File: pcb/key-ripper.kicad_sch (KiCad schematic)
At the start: 205 parts, among them J1 Conn_01x03, SW1 ESC, SW10 F9, SW11 F10, SW12 F11, SW13 F12, SW14 TILDE, SW15 1, SW16 2, SW17 3, SW18 4, SW19 5, SW2 F1, SW20 6, SW21 7, SW22 8, SW23 9, SW24 0, SW25 -, SW26 =, SW27 BACKSPACE, SW28 TAB, SW29 Q, SW3 F2, SW30 W, SW31 E, SW32 R, SW33 T, SW34 Y, SW35 U, SW36 I, SW37 O, SW38 P, SW39 [, SW4 F3, SW40 ], SW41 \, SW42 CAPS, SW43 A, SW44 S, SW45 D, SW46 F, SW47 G, SW48 H, SW49 J, SW5 F4, SW50 K, SW51 L, SW52 ;, SW53 ', SW54 ENTER, SW55 L_SHIFT, SW56 Z, SW57 X, SW58 C, SW59 V, SW6 F5, SW60 B, SW61 N, SW62 M, SW63 ,, SW64 ., SW65 /, SW66 UP, SW67 FN, SW68 BL_CTRL, SW69 L_ALT, SW7 F6, SW70 L_CMD, SW71 SPACE, SW72 R_CMD, SW73 LEFT, SW74 DOWN, SW75 RIGHT, SW8 F7, SW9 F8, U1 RP2040, U2 TYPE-C-31-M-12, U3 XC6206PxxxMR, U4 W25Q128JVS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

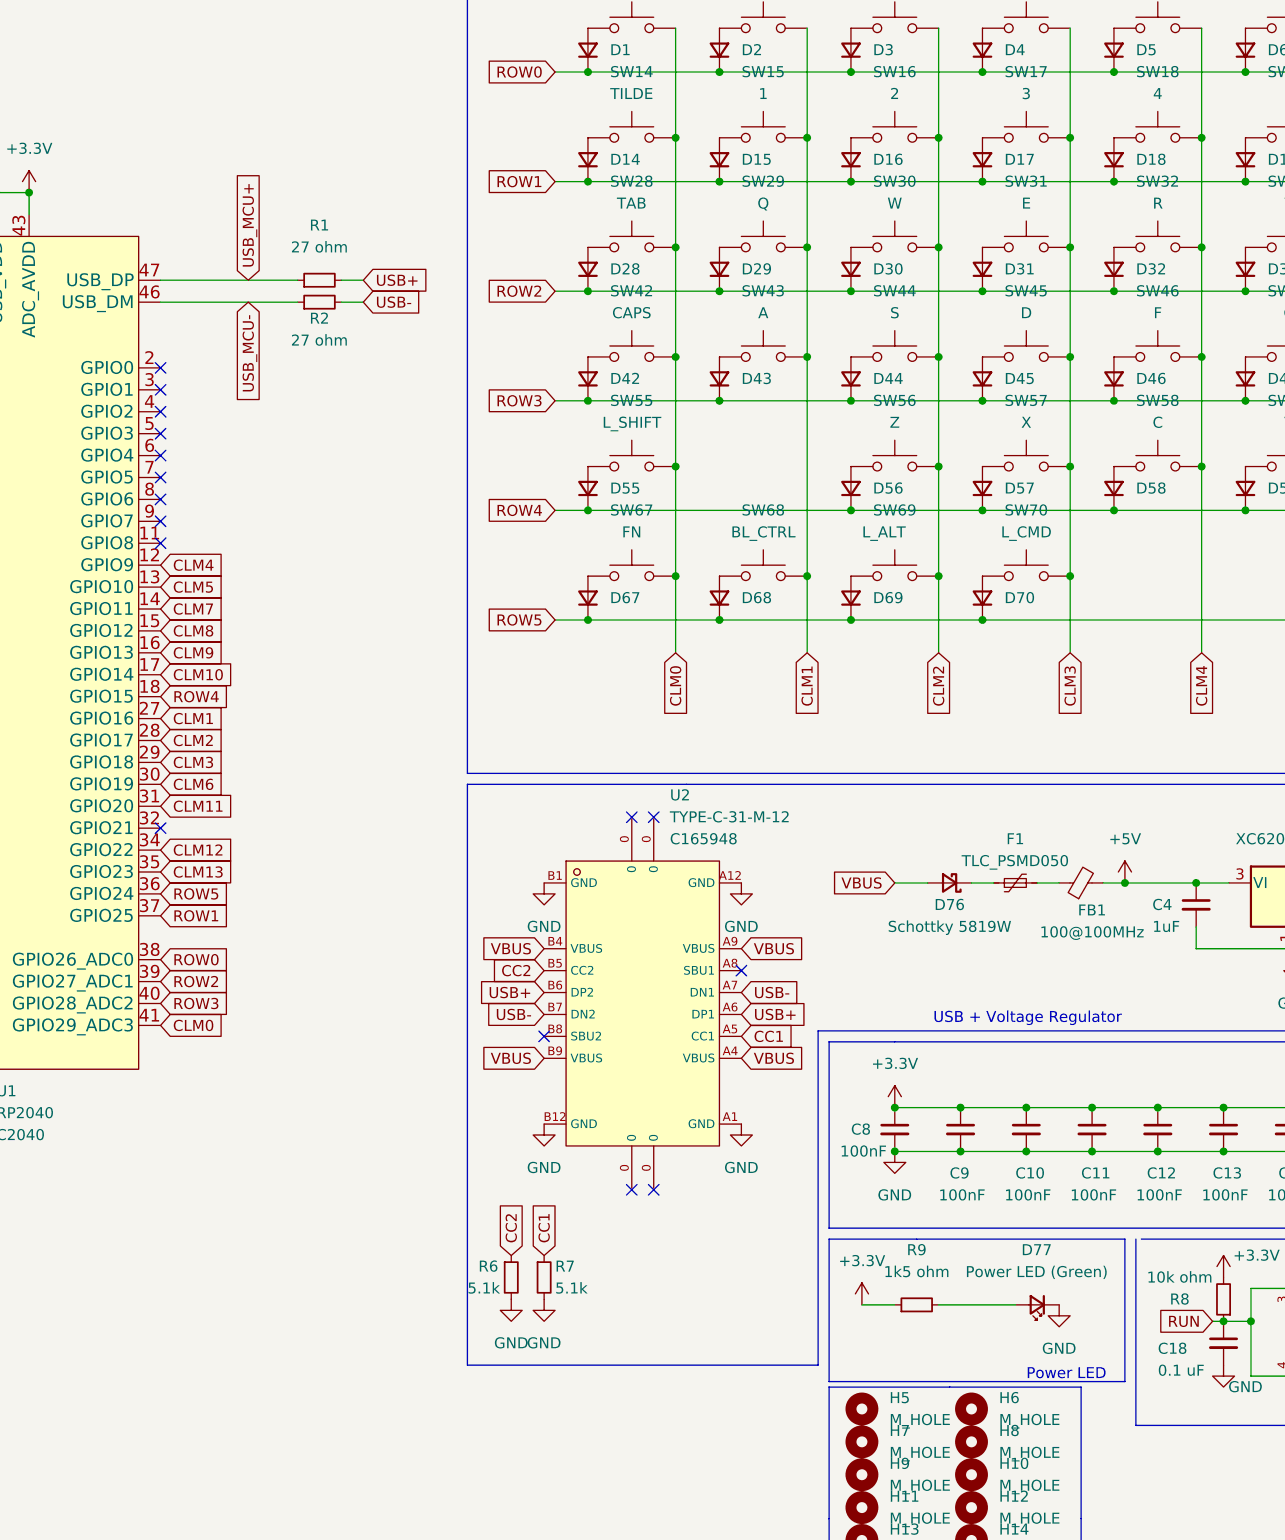
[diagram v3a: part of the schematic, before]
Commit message: Turn GPIO 2 into a user LED
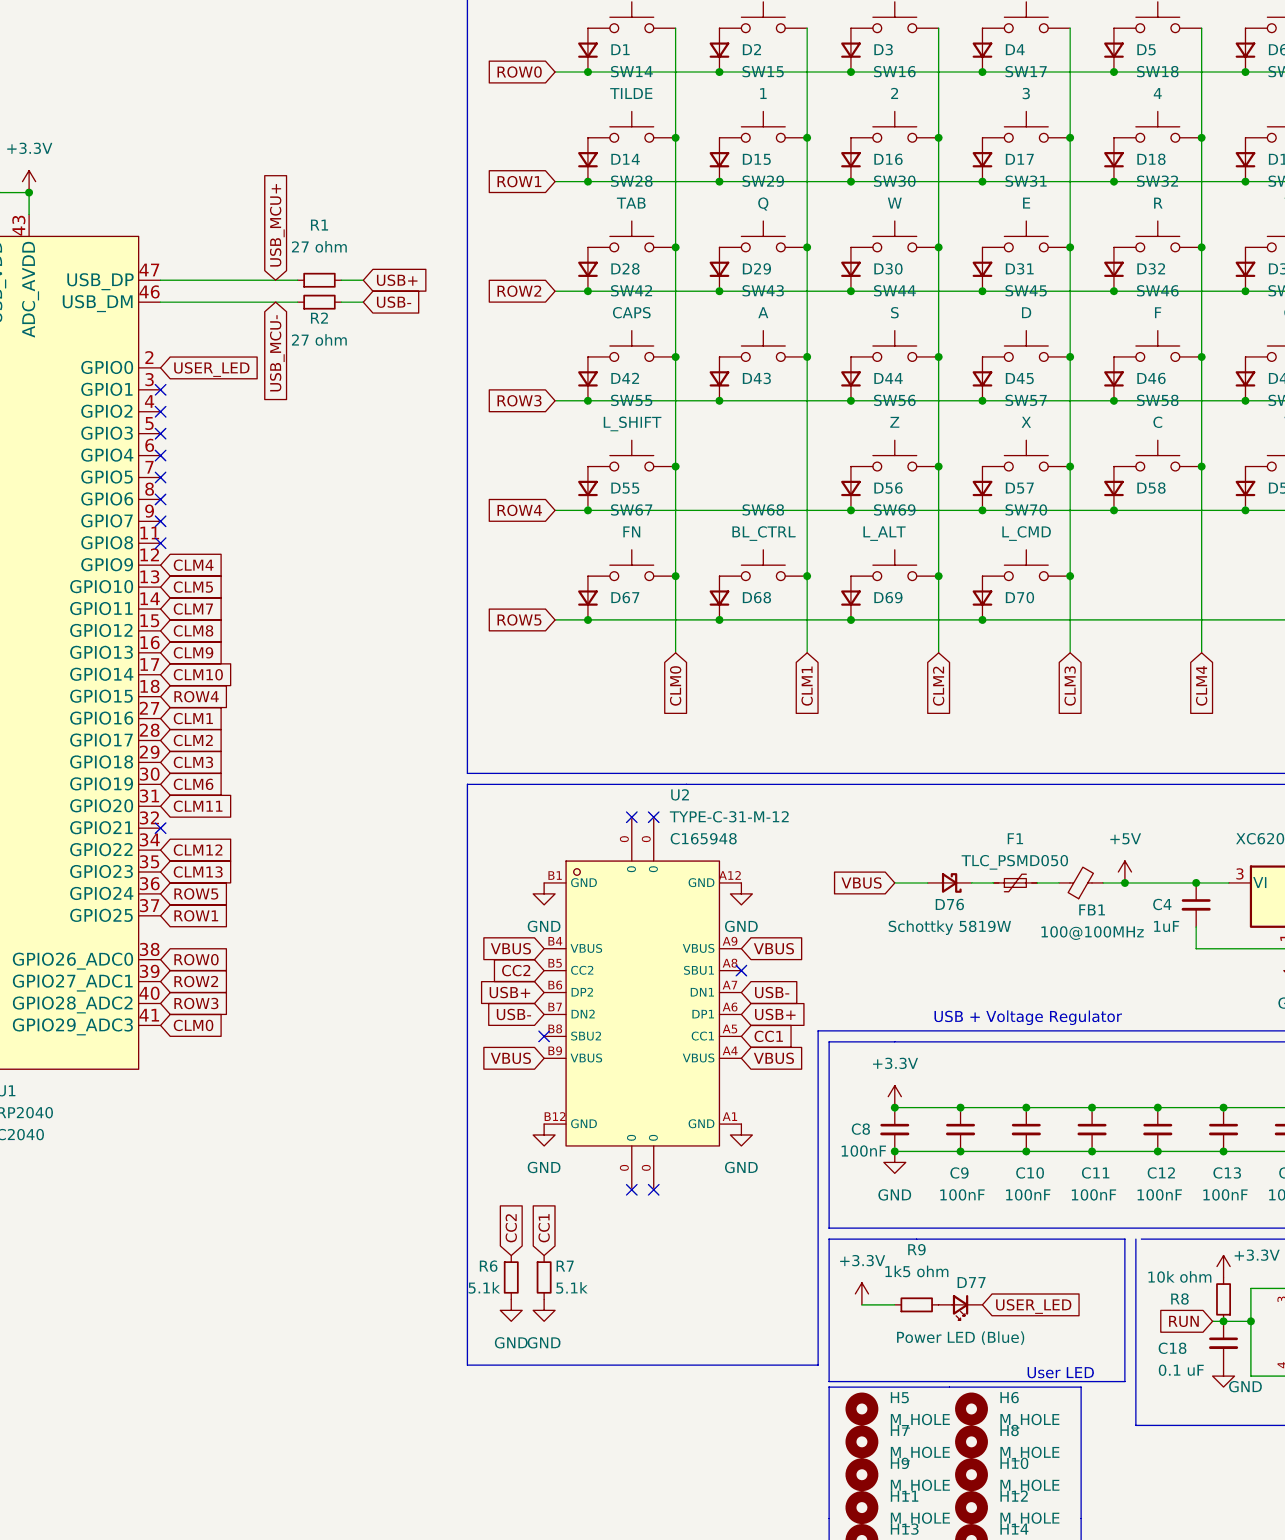
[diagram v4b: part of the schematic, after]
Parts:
- D77: value Power LED (Green) -> Power LED (Blue)
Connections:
- net GND: no longer D77.1 (K)
- net USER_LED: now reaches U1.2 (GPIO0)
- net USER_LED: now also D77.1 (K)
- no-connect marks 16 -> 15
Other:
- note added: "User LED"
- note removed: "Power LED"
- moved on the sheet: D77
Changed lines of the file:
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@@
   (no_connect (at -22.86 73.66))
   (no_connect (at -22.86 71.12))
-  (no_connect (at -22.86 63.5))
   (no_connect (at -22.86 116.84))
   (no_connect (at -22.86 68.58))
@@
     (stroke (width 0) (type default) (color 0 0 0 0))
   )
-  (wire (pts (xy 67.31 172.085) (xy 76.2 172.085))
-    (stroke (width 0) (type default) (color 0 0 0 0))
-  )
   (wire (pts (xy 118.11 54.61) (xy 133.35 54.61))
     (stroke (width 0) (type default) (color 0 0 0 0))
@@
     (effects (font (size 1.27 1.27)) (justify left bottom))
   )
-  (text "Power LED" (at 77.47 180.975 0)
+  (text "User LED" (at 77.47 180.975 0)
     (effects (font (size 1.27 1.27)) (justify left bottom))
   )
@@
     )
   )
-  (global_label "USB_MCU+" (shape input) (at -12.7 53.34 90) (fields_autoplaced)
+  (global_label "USB_MCU+" (shape input) (at -9.525 53.34 90) (fields_autoplaced)
     (effects (font (size 1.27 1.27)) (justify left))
-    (property "Intersheet References" "${INTERSHEET_REFS}" (id 0) (at -12.7794 40.525 90)
+    (property "Intersheet References" "${INTERSHEET_REFS}" (id 0) (at -9.6044 40.525 90)
       (effects (font (size 1.27 1.27)) (justify left) hide)
     )
@@
     )
   )
+  (global_label "USER_LED" (shape input) (at -22.86 63.5 0) (fields_autoplaced)
+    (effects (font (size 1.27 1.27)) (justify left))
+    (property "Intersheet References" "${INTERSHEET_REFS}" (id 0) (at -11.0731 63.4206 0)
+      (effects (font (size 1.27 1.27)) (justify left) hide)
+    )
+  )
   (global_label "CLM4" (shape input) (at 97.79 96.52 270) (fields_autoplaced)
     (effects (font (size 1.27 1.27)) (justify right))
@@
     )
   )
-  (global_label "USB_MCU-" (shape input) (at -12.7 55.88 270) (fields_autoplaced)
+  (global_label "USB_MCU-" (shape input) (at -9.525 55.88 270) (fields_autoplaced)
     (effects (font (size 1.27 1.27)) (justify right))
-    (property "Intersheet References" "${INTERSHEET_REFS}" (id 0) (at -12.7794 68.695 90)
+    (property "Intersheet References" "${INTERSHEET_REFS}" (id 0) (at -9.6044 68.695 90)
       (effects (font (size 1.27 1.27)) (justify right) hide)
     )
@@
     )
   )
+  (global_label "USER_LED" (shape input) (at 72.39 172.085 0) (fields_autoplaced)
+    (effects (font (size 1.27 1.27)) (justify left))
+    (property "Intersheet References" "${INTERSHEET_REFS}" (id 0) (at 84.1769 172.0056 0)
+      (effects (font (size 1.27 1.27)) (justify left) hide)
+    )
+  )
   (global_label "RUN" (shape input) (at -86.36 116.84 180) (fields_autoplaced)
     (effects (font (size 1.27 1.27)) (justify right))
@@
     (pin "2")
   )
-  (symbol (lib_id "power:GND") (at 81.28 172.085 0) (unit 1)
-    (in_bom yes) (on_board yes) (fields_autoplaced)
-    (property "Reference" "#PWR031" (id 0) (at 81.28 178.435 0)
-      (effects (font (size 1.27 1.27)) hide)
-    )
-    (property "Value" "GND" (id 1) (at 81.28 177.165 0))
-    (property "Footprint" "" (id 2) (at 81.28 172.085 0)
-      (effects (font (size 1.27 1.27)) hide)
-    )
-    (property "Datasheet" "" (id 3) (at 81.28 172.085 0)
-      (effects (font (size 1.27 1.27)) hide)
-    )
-    (pin "1")
-  )
   (symbol (lib_id "Device:D_Small") (at 87.63 52.07 90) (unit 1)
     (in_bom yes) (on_board yes)
@@
     (pin "2")
   )
-  (symbol (lib_id "Device:LED_Small") (at 78.74 172.085 180) (unit 1)
-    (in_bom yes) (on_board yes) (fields_autoplaced)
-    (property "Reference" "D77" (id 0) (at 78.6765 165.735 0))
-    (property "Value" "Power LED (Green)" (id 1) (at 78.6765 168.275 0))
-    (property "Footprint" "LED_SMD:LED_0805_2012Metric" (id 2) (at 78.74 172.085 90)
+  (symbol (lib_id "Device:LED_Small") (at 69.85 172.085 180) (unit 1)
+    (in_bom yes) (on_board yes)
+    (property "Reference" "D77" (id 0) (at 71.12 169.545 0))
+    (property "Value" "Power LED (Blue)" (id 1) (at 69.85 175.895 0))
+    (property "Footprint" "LED_SMD:LED_0805_2012Metric" (id 2) (at 69.85 172.085 90)
       (effects (font (size 1.27 1.27)) hide)
     )
-    (property "Datasheet" "~" (id 3) (at 78.74 172.085 90)
+    (property "Datasheet" "~" (id 3) (at 69.85 172.085 90)
       (effects (font (size 1.27 1.27)) hide)
     )
@@
       (reference "#PWR030") (unit 1) (value "+3.3V") (footprint "")
     )
-    (path "/2cb114ba-1938-4b9e-8b57-e5a613f9de7f"
-      (reference "#PWR031") (unit 1) (value "GND") (footprint "")
-    )
     (path "/cdc9f184-a98f-4194-a3dd-613cbf52294c"
       (reference "#PWR032") (unit 1) (value "GND") (footprint "")
@@
     )
     (path "/f01c71a7-46e2-4e2a-a493-f3aa185e40b3"
-      (reference "D77") (unit 1) (value "Power LED (Green)") (footprint "LED_SMD:LED_0805_2012Metric")
+      (reference "D77") (unit 1) (value "Power LED (Blue)") (footprint "LED_SMD:LED_0805_2012Metric")
     )
     (path "/b1435a2c-b9ff-468c-9db6-b6d7bca7609e"

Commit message: Use the soldered MX footprint instead of kailh hotswap footprint
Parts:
- SW1, SW10, SW11, SW12, SW13, SW14, SW15, SW16, SW17, SW18, SW19, SW2, SW20, SW21, SW22, SW23, SW24, SW25, SW26, SW29, SW3, SW30, SW31, SW32, SW33, SW34, SW35, SW36, SW37, SW38, SW39, SW4, SW40, SW43, SW44, SW45, SW46, SW47, SW48, SW49, SW5, SW50, SW51, SW52, SW53, SW56, SW57, SW58, SW59, SW6, SW60, SW61, SW62, SW63, SW64, SW65, SW66, SW67, SW68, SW69, SW7, SW73, SW74, SW75, SW8, SW9: footprint Switch_Keyboard_Hotswap_Kailh:SW_Hotswap_Kailh_MX_1.00u -> Switch_Keyboard_Cherry_MX:SW_Cherry_MX_PCB_1.00u
- SW27: footprint Switch_Keyboard_Hotswap_Kailh:SW_Hotswap_Kailh_MX_2.00u -> Switch_Keyboard_Cherry_MX:SW_Cherry_MX_PCB_2.00u
- SW28, SW41: footprint Switch_Keyboard_Hotswap_Kailh:SW_Hotswap_Kailh_MX_1.50u -> Switch_Keyboard_Cherry_MX:SW_Cherry_MX_PCB_1.50u
- SW42: footprint Switch_Keyboard_Hotswap_Kailh:SW_Hotswap_Kailh_MX_1.75u -> Switch_Keyboard_Cherry_MX:SW_Cherry_MX_PCB_1.75u
- SW54, SW55: footprint Switch_Keyboard_Hotswap_Kailh:SW_Hotswap_Kailh_MX_2.25u -> Switch_Keyboard_Cherry_MX:SW_Cherry_MX_PCB_2.25u
- SW70: footprint Switch_Keyboard_Hotswap_Kailh:SW_Hotswap_Kailh_MX_1.25u -> Switch_Keyboard_Cherry_MX:SW_Cherry_MX_PCB_1.00u
- SW71: footprint Switch_Keyboard_Hotswap_Kailh:SW_Hotswap_Kailh_MX_6.25u -> Switch_Keyboard_Cherry_MX:SW_Cherry_MX_PCB_6.25u
- SW72: footprint Switch_Keyboard_Hotswap_Kailh:SW_Hotswap_Kailh_MX_1.25u -> Switch_Keyboard_Cherry_MX:SW_Cherry_MX_PCB_1.25u

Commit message: Update switch footprints, adjust silkscreens
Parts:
- SW70: footprint Switch_Keyboard_Cherry_MX:SW_Cherry_MX_PCB_1.00u -> Switch_Keyboard_Cherry_MX:SW_Cherry_MX_PCB_1.25u
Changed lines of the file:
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@@
     (property "Reference" "SW70" (id 0) (at 77.47 80.01 0))
     (property "Value" "L_CMD" (id 1) (at 77.47 82.55 0))
-    (property "Footprint" "Switch_Keyboard_Cherry_MX:SW_Cherry_MX_PCB_1.00u" (id 2) (at 77.47 82.55 0)
+    (property "Footprint" "Switch_Keyboard_Cherry_MX:SW_Cherry_MX_PCB_1.25u" (id 2) (at 77.47 82.55 0)
       (effects (font (size 1.27 1.27)) hide)
     )
@@
     )
     (path "/e33778d5-cb40-42f9-9ae6-7a40987eefdc"
-      (reference "SW70") (unit 1) (value "L_CMD") (footprint "Switch_Keyboard_Cherry_MX:SW_Cherry_MX_PCB_1.00u")
+      (reference "SW70") (unit 1) (value "L_CMD") (footprint "Switch_Keyboard_Cherry_MX:SW_Cherry_MX_PCB_1.25u")
     )
     (path "/3194f8fe-c356-4c60-bba2-89cf59e136ba"

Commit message: Update stabilizer footprints
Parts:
- H1, H3, H4: footprint Mounting_Keyboard_Stabilizer:Stabilizer_Cherry_MX_2.00u -> bschwind_stabilizers:cherry_mx_stabilizer_2.00u
- H2: footprint Mounting_Keyboard_Stabilizer:Stabilizer_Cherry_MX_6.25u -> bschwind_stabilizers:cherry_mx_stabilizer_6.25u
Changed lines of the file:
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@@
       (effects (font (size 1.27 1.27)) (justify left))
     )
-    (property "Footprint" "Mounting_Keyboard_Stabilizer:Stabilizer_Cherry_MX_6.25u" (id 2) (at 128.27 172.72 0)
+    (property "Footprint" "bschwind_stabilizers:cherry_mx_stabilizer_6.25u" (id 2) (at 128.27 172.72 0)
       (effects (font (size 1.27 1.27)) hide)
     )
@@
       (effects (font (size 1.27 1.27)) (justify left))
     )
-    (property "Footprint" "Mounting_Keyboard_Stabilizer:Stabilizer_Cherry_MX_2.00u" (id 2) (at 128.27 167.64 0)
+    (property "Footprint" "bschwind_stabilizers:cherry_mx_stabilizer_2.00u" (id 2) (at 128.27 167.64 0)
       (effects (font (size 1.27 1.27)) hide)
     )
@@
       (effects (font (size 1.27 1.27)) (justify left))
     )
-    (property "Footprint" "Mounting_Keyboard_Stabilizer:Stabilizer_Cherry_MX_2.00u" (id 2) (at 128.27 182.88 0)
+    (property "Footprint" "bschwind_stabilizers:cherry_mx_stabilizer_2.00u" (id 2) (at 128.27 182.88 0)
       (effects (font (size 1.27 1.27)) hide)
     )
@@
       (effects (font (size 1.27 1.27)) (justify left))
     )
-    (property "Footprint" "Mounting_Keyboard_Stabilizer:Stabilizer_Cherry_MX_2.00u" (id 2) (at 128.27 177.8 0)
+    (property "Footprint" "bschwind_stabilizers:cherry_mx_stabilizer_2.00u" (id 2) (at 128.27 177.8 0)
       (effects (font (size 1.27 1.27)) hide)
     )
@@
     )
     (path "/179eb089-facc-4792-bd04-c114d0661855"
-      (reference "H1") (unit 1) (value "L_SHIFT_STABILIZER") (footprint "Mounting_Keyboard_Stabilizer:Stabilizer_Cherry_MX_2.00u")
+      (reference "H1") (unit 1) (value "L_SHIFT_STABILIZER") (footprint "bschwind_stabilizers:cherry_mx_stabilizer_2.00u")
     )
     (path "/145c11b9-1bdc-4693-9d2e-9955fd7b97f7"
-      (reference "H2") (unit 1) (value "SPACE_STABILIZER") (footprint "Mounting_Keyboard_Stabilizer:Stabilizer_Cherry_MX_6.25u")
+      (reference "H2") (unit 1) (value "SPACE_STABILIZER") (footprint "bschwind_stabilizers:cherry_mx_stabilizer_6.25u")
     )
     (path "/90203188-a65e-466d-a2ed-515dc2020f60"
-      (reference "H3") (unit 1) (value "ENTER_STABILIZER") (footprint "Mounting_Keyboard_Stabilizer:Stabilizer_Cherry_MX_2.00u")
+      (reference "H3") (unit 1) (value "ENTER_STABILIZER") (footprint "bschwind_stabilizers:cherry_mx_stabilizer_2.00u")
     )
     (path "/8ef6d468-ac05-41d5-8054-7dff4a149731"
-      (reference "H4") (unit 1) (value "BACKSPACE_STABILIZER") (footprint "Mounting_Keyboard_Stabilizer:Stabilizer_Cherry_MX_2.00u")
+      (reference "H4") (unit 1) (value "BACKSPACE_STABILIZER") (footprint "bschwind_stabilizers:cherry_mx_stabilizer_2.00u")
     )
     (path "/5c0b23f2-203a-4182-94e3-5277128c45dc"

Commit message: Update switch footprints
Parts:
- SW1, SW10, SW11, SW12, SW13, SW14, SW15, SW16, SW17, SW18, SW19, SW2, SW20, SW21, SW22, SW23, SW24, SW25, SW26, SW29, SW3, SW30, SW31, SW32, SW33, SW34, SW35, SW36, SW37, SW38, SW39, SW4, SW40, SW43, SW44, SW45, SW46, SW47, SW48, SW49, SW5, SW50, SW51, SW52, SW53, SW56, SW57, SW58, SW59, SW6, SW60, SW61, SW62, SW63, SW64, SW65, SW66, SW67, SW68, SW69, SW7, SW73, SW74, SW75, SW8, SW9: footprint Switch_Keyboard_Cherry_MX:SW_Cherry_MX_PCB_1.00u -> bschwind_switches_cherry_mx:cherry_mx_5_pin_1.00u
- SW27: footprint Switch_Keyboard_Cherry_MX:SW_Cherry_MX_PCB_2.00u -> bschwind_switches_cherry_mx:cherry_mx_5_pin_2.00u
- SW28, SW41: footprint Switch_Keyboard_Cherry_MX:SW_Cherry_MX_PCB_1.50u -> bschwind_switches_cherry_mx:cherry_mx_5_pin_1.50u
- SW42: footprint Switch_Keyboard_Cherry_MX:SW_Cherry_MX_PCB_1.75u -> bschwind_switches_cherry_mx:cherry_mx_5_pin_1.75u
- SW54, SW55: footprint Switch_Keyboard_Cherry_MX:SW_Cherry_MX_PCB_2.25u -> bschwind_switches_cherry_mx:cherry_mx_5_pin_2.25u
- SW70, SW72: footprint Switch_Keyboard_Cherry_MX:SW_Cherry_MX_PCB_1.25u -> bschwind_switches_cherry_mx:cherry_mx_5_pin_1.25u
- SW71: footprint Switch_Keyboard_Cherry_MX:SW_Cherry_MX_PCB_6.25u -> bschwind_switches_cherry_mx:cherry_mx_5_pin_6.25u
